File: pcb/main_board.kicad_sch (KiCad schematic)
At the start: 9 parts, among them J1 HDMI Breakout, J2 HDMI Breakout, J5 USB_A, J6 USB_A, J7 USB_A, SW1 SW_RST, U1 PGA2350, U2 CH334F

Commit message: Continue work on PCBs.
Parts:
- J5, J6, J7: footprint (none) -> Connector_USB:USB_A_Molex_67643_Horizontal
- SW1: footprint (none) -> Button_Switch_THT:SW_PUSH_6mm
- SW2: renamed from SW_BOOT; value SW_Push -> SW_BOOT; footprint (none) -> Button_Switch_THT:SW_PUSH_6mm
- U2: footprint (none) -> excelsior:USB_Hub
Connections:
- net CS0: now also J1.02 (P02), J2.02 (P02); no longer J1.04 (P04), J2.04 (P04)
- net MISO: now also J1.01 (P01), J2.01 (P01); no longer J1.02 (P02), J2.02 (P02)
- net MOSI: now also J1.05 (P05), J2.05 (P05); no longer J1.08 (P08), J2.08 (P08)
- net SCK: now also J1.03 (P03), J2.03 (P03); no longer J1.06 (P06), J2.06 (P06)
- net SDA: now reaches J1.07 (P07)
- net SDA: now also J2.07 (P07), U1.04 (GP04)
- net SCL: now reaches J1.09 (P09)
- net SCL: now also J2.09 (P09), U1.05 (GP05)
- net CS4: now reaches J1.10 (P10)
- net CS4: now also J2.10 (P10), U1.44 (GP44)
- net INTA1: now reaches J1.11 (P11)
- net INTA1: now also J2.11 (P11), U1.06 (GP06)
- net CS5: now reaches J1.12 (P12)
- net CS5: now also J2.12 (P12), U1.45 (GP45)
- net INTB1: now reaches J1.13 (P13)
- net INTB1: now also J2.13 (P13), U1.07 (GP07)
- net CS6: now reaches J1.14 (P14)
- net CS6: now also J2.14 (P14), U1.46 (GP46)
- net INTA2: now reaches J1.15 (P15)
- net INTA2: now also J2.15 (P15), U1.08 (GP08)
- net CS7: now reaches J1.16 (P16)
- net CS7: now also J2.16 (P16), U1.47 (GP47)
- net INTB2: now reaches U1.09 (GP09)
- net INTB2: now also J1.19 (P19), J2.19 (P19)
- net R00: now reaches U1.10 (GP10)
- net R01: now reaches U1.11 (GP11)
- net R02: now reaches U1.12 (GP12)
- net R03: now reaches U1.13 (GP13)
- net R04: now reaches U1.14 (GP14)
- net R05: now reaches U1.15 (GP15)
- net R06: now reaches U1.16 (GP16)
- net C00: now reaches U1.17 (GP17)
- net C01: now reaches U1.18 (GP18)
- net C02: now reaches U1.19 (GP19)
- net C03: now reaches U1.20 (GP20)
- net C04: now reaches U1.21 (GP21)
- net C05: now reaches U1.22 (GP22)
- net C06: now reaches U1.23 (GP23)
- net C07: now reaches U1.24 (GP24)
- net C08: now reaches U1.25 (GP25)
- net C09: now reaches U1.26 (GP26)
- net C10: now reaches U1.27 (GP27)
- net C11: now reaches U1.28 (GP28)
- net C12: now reaches U1.29 (GP29)
- net C13: now reaches U1.30 (GP30)
- net GP31: now reaches U1.31 (GP31)
- net GP32: now reaches U1.32 (GP32)
- net GP33: now reaches U1.33 (GP33)
- net GP34: now reaches U1.34 (GP34)
- net GP35: now reaches U1.35 (GP35)
- net GP36: now reaches U1.36 (GP36)
- net GP37: now reaches U1.37 (GP37)
- net GP38: now reaches U1.38 (GP38)
- net GP39: now reaches U1.39 (GP39)
- net CS8: now reaches U1.40 (GP40)
- net CS1: now reaches U1.41 (GP41)
- net CS1: now also J1.04 (P04), J2.04 (P04)
- net CS2: now reaches U1.42 (GP42)
- net CS2: now also J1.06 (P06), J2.06 (P06)
- net CS3: now reaches U1.43 (GP43)
- net CS3: now also J1.08 (P08), J2.08 (P08)
- no-connect marks 0 -> 5
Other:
- moved on the sheet: J1, J2

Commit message: Continue work on PCBs.
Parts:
- J1, J2: value HDMI Breakout -> Pogo Pin Connector; footprint excelsior:HDMI_Breakout -> Connector_PinHeader_2.54mm:PinHeader_1x12_P2.54mm_Vertical; symbol excelsior:HDMI_Breakout -> Connector_Generic:Conn_01x12
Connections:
- net CS0: now also J1.10 (Pin_10), J2.10 (Pin_10); no longer J1.02 (P02), J2.02 (P02)
- net CS1: now also J1.11 (Pin_11), J2.11 (Pin_11); no longer J1.04 (P04), J2.04 (P04)
- net CS2: now also J1.12 (Pin_12), J2.12 (Pin_12); no longer J1.06 (P06), J2.06 (P06)
- net CS3: no longer J1.08 (P08), J2.08 (P08)
- net CS4: no longer J1.10 (P10), J2.10 (P10)
- net CS5: no longer J1.12 (P12), J2.12 (P12)
- net CS6: no longer J1.14 (P14), J2.14 (P14)
- net CS7: no longer J1.16 (P16), J2.16 (P16)
- net GND: no longer J1.G (GND), J2.G (GND)
- net INTA1: now also J1.6 (Pin_6), J2.6 (Pin_6); no longer J1.11 (P11), J2.11 (P11)
- net INTA2: now also J1.8 (Pin_8), J2.8 (Pin_8); no longer J1.15 (P15), J2.15 (P15)
- net INTB1: now also J1.7 (Pin_7), J2.7 (Pin_7); no longer J1.13 (P13), J2.13 (P13)
- net INTB2: now also J1.9 (Pin_9), J2.9 (Pin_9); no longer J1.19 (P19), J2.19 (P19)
- net MISO: now also J1.1 (Pin_1), J2.1 (Pin_1); no longer J1.01 (P01), J2.01 (P01)
- net MOSI: now also J1.3 (Pin_3), J2.3 (Pin_3); no longer J1.05 (P05), J2.05 (P05)
- net SCK: now also J1.2 (Pin_2), J2.2 (Pin_2); no longer J1.03 (P03), J2.03 (P03)
- net SCL: now also J1.5 (Pin_5), J2.5 (Pin_5); no longer J1.09 (P09), J2.09 (P09)
- net SDA: now also J1.4 (Pin_4), J2.4 (Pin_4); no longer J1.07 (P07), J2.07 (P07)
- net VBUS: no longer J1.00 (VBUS), J2.00 (VBUS)

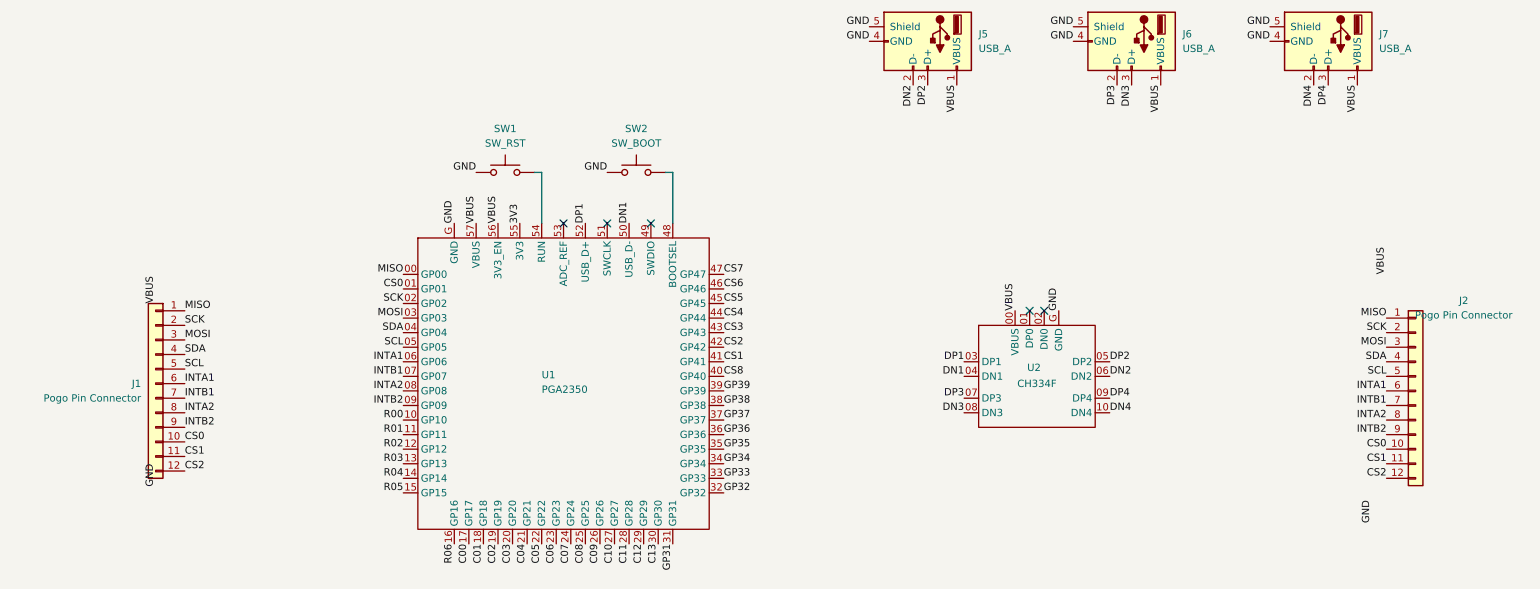
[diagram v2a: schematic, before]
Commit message: - Update main Readme. - Add folders for case CAD and KMK files. - In the PCBs, fix VBUS and GND being removed from connectors. - Add PCB readme.
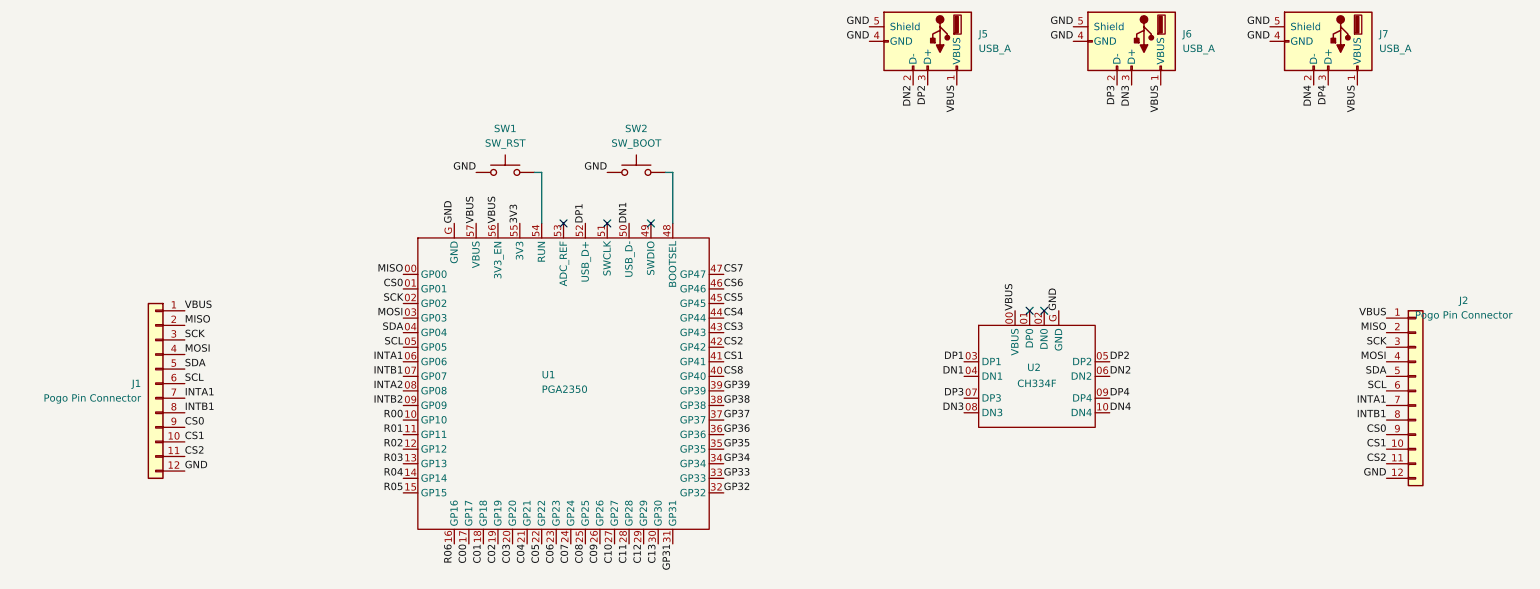
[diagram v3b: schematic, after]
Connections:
- net CS0: now also J1.9 (Pin_9), J2.9 (Pin_9); no longer J1.10 (Pin_10), J2.10 (Pin_10)
- net CS1: now also J1.10 (Pin_10), J2.10 (Pin_10); no longer J1.11 (Pin_11), J2.11 (Pin_11)
- net CS2: now also J1.11 (Pin_11), J2.11 (Pin_11); no longer J1.12 (Pin_12), J2.12 (Pin_12)
- net GND: now also J1.12 (Pin_12), J2.12 (Pin_12)
- net INTA1: now also J1.7 (Pin_7), J2.7 (Pin_7); no longer J1.6 (Pin_6), J2.6 (Pin_6)
- net INTA2: no longer J1.8 (Pin_8), J2.8 (Pin_8)
- net INTB1: now also J1.8 (Pin_8), J2.8 (Pin_8); no longer J1.7 (Pin_7), J2.7 (Pin_7)
- net INTB2: no longer J1.9 (Pin_9), J2.9 (Pin_9)
- net MISO: now also J1.2 (Pin_2), J2.2 (Pin_2); no longer J1.1 (Pin_1), J2.1 (Pin_1)
- net MOSI: now also J1.4 (Pin_4), J2.4 (Pin_4); no longer J1.3 (Pin_3), J2.3 (Pin_3)
- net SCK: now also J1.3 (Pin_3), J2.3 (Pin_3); no longer J1.2 (Pin_2), J2.2 (Pin_2)
- net SCL: now also J1.6 (Pin_6), J2.6 (Pin_6); no longer J1.5 (Pin_5), J2.5 (Pin_5)
- net SDA: now also J1.5 (Pin_5), J2.5 (Pin_5); no longer J1.4 (Pin_4), J2.4 (Pin_4)
- net VBUS: now also J1.1 (Pin_1), J2.1 (Pin_1)
